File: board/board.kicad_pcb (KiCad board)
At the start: 2 copper layers, 44.3 x 82.8 mm, 20 parts, among them J1 port attiny, J10 BMS Bat +, J11 BMS Bat gnd, J12 BMS out -, J13 BMS in +5v, J14 BMS in gnd, J2 alim attiny, J24 port 3-C265421, J3 alim mp3, J4 hp mp3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

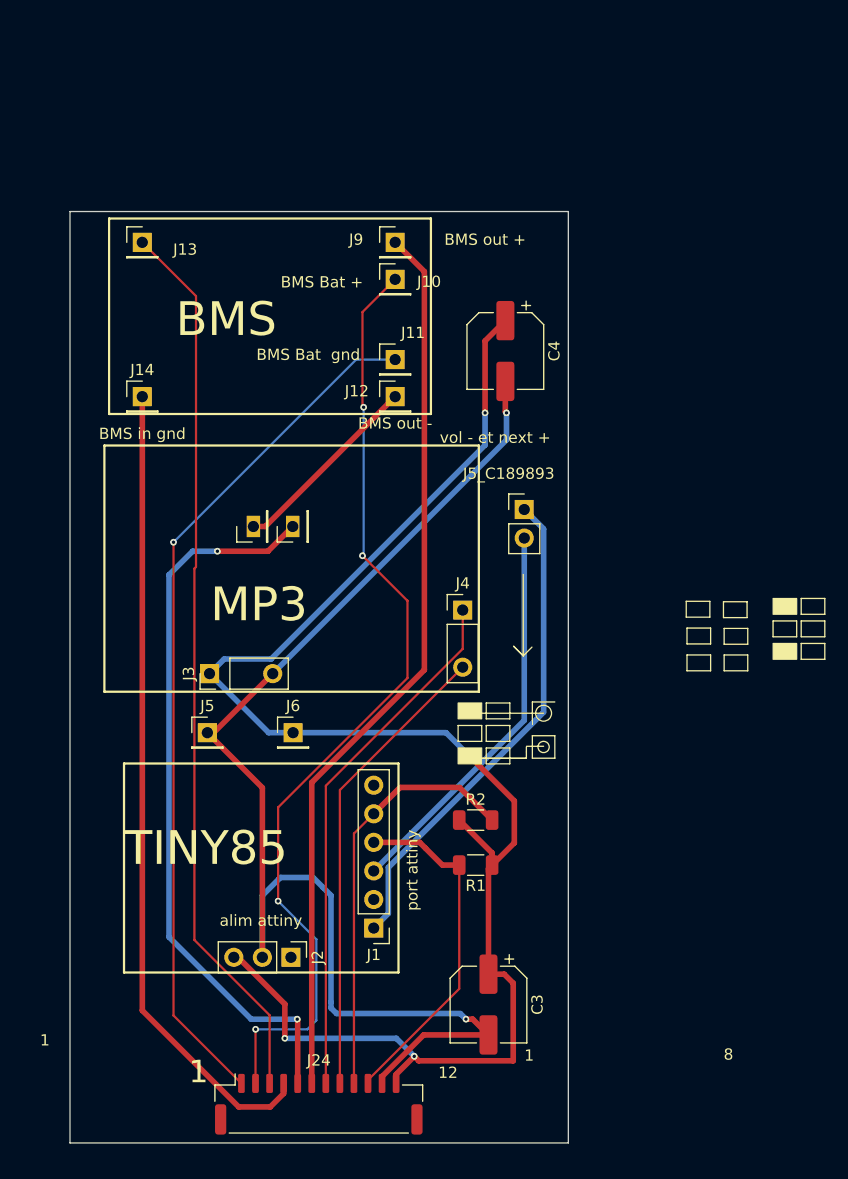
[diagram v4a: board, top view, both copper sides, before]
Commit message: mise a jour marquage pcb et ajout programation tiny dans le source
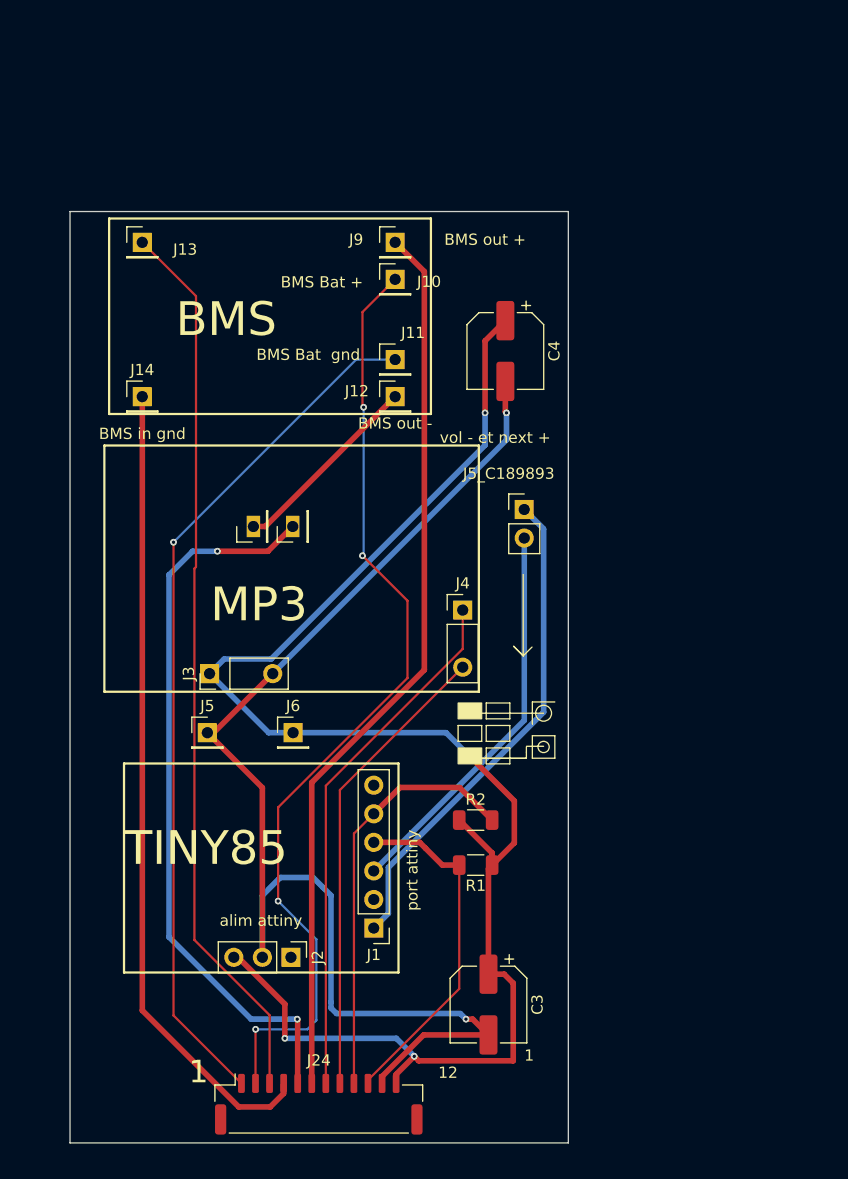
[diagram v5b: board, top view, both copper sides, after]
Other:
- board text removed: "8"
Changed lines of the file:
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@@
-		(layer "F.SilkS")
-	)
-	(gr_rect
-		(start 126.9 74.295)
-		(end 129 75.705)
-		(stroke
-			(width 0.1)
-			(type default)
-		)
-		(fill no)
 		(layer "F.SilkS")
 	)
@@
 		(layer "F.SilkS")
 	)
-	(gr_rect
-		(start 126.9 72.295)
-		(end 129 73.705)
-		(stroke
-			(width 0.1)
-			(type default)
-		)
-		(fill no)
-		(layer "F.SilkS")
-	)
-	(gr_rect
-		(start 116.75 74.93)
-		(end 118.85 76.34)
-		(stroke
-			(width 0.1)
-			(type default)
-		)
-		(fill no)
-		(layer "F.SilkS")
-	)
-	(gr_rect
-		(start 124.4 72.295)
-		(end 126.5 73.705)
-		(stroke
-			(width 0.1)
-			(type solid)
-		)
-		(fill yes)
-		(layer "F.SilkS")
-	)
 	(gr_circle
 		(center 104 82.5)
@@
 	)
 	(gr_rect
-		(start 124.4 76.295)
-		(end 126.5 77.705)
-		(stroke
-			(width 0.1)
-			(type solid)
-		)
-		(fill yes)
-		(layer "F.SilkS")
-	)
-	(gr_rect
-		(start 124.4 74.295)
-		(end 126.5 75.705)
-		(stroke
-			(width 0.1)
-			(type default)
-		)
-		(fill no)
-		(layer "F.SilkS")
-	)
-	(gr_rect
 		(start 98.9 83.59)
 		(end 101 85)
@@
 		(layer "F.SilkS")
 	)
-	(gr_rect
-		(start 120.05 77.32)
-		(end 122.15 78.73)
-		(stroke
-			(width 0.1)
-			(type default)
-		)
-		(fill no)
-		(layer "F.SilkS")
-	)
-	(gr_rect
-		(start 126.9 76.295)
-		(end 129 77.705)
-		(stroke
-			(width 0.1)
-			(type default)
-		)
-		(fill no)
-		(layer "F.SilkS")
-	)
 	(gr_line
 		(start 105 81.5)
@@
 		(layer "F.SilkS")
 	)
-	(gr_rect
-		(start 116.68 72.55)
-		(end 118.78 73.96)
-		(stroke
-			(width 0.1)
-			(type default)
-		)
-		(fill no)
-		(layer "F.SilkS")
-	)
-	(gr_rect
-		(start 116.75 77.32)
-		(end 118.85 78.73)
-		(stroke
-			(width 0.1)
-			(type default)
-		)
-		(fill no)
-		(layer "F.SilkS")
-	)
 	(gr_line
 		(start 102.47 85.95)
@@
 	)
 	(gr_rect
-		(start 119.99 72.59)
-		(end 122.09 74)
-		(stroke
-			(width 0.1)
-			(type default)
-		)
-		(fill no)
-		(layer "F.SilkS")
-	)
-	(gr_rect
 		(start 65.375 38.52)
 		(end 93.985 55.9)
@@
 		(layer "F.SilkS")
 	)
-	(gr_rect
-		(start 120.05 74.96)
-		(end 122.15 76.37)
-		(stroke
-			(width 0.1)
-			(type default)
-		)
-		(fill no)
-		(layer "F.SilkS")
-	)
 	(gr_line
 		(start 102.19 70.15)
@@
 		(layer "Edge.Cuts")
 	)
-	(gr_text "1"
-		(at 59.23 112.16 0)
-		(layer "F.SilkS")
-		(effects
-			(font
-				(size 1 1)
-				(thickness 0.1)
-			)
-			(justify left bottom)
-		)
-	)
 	(gr_text "MP3"
 		(at 74.38 74.6 0)
@@
 				(thickness 0.1)
 			)
-			(justify left bottom)
-		)
-	)
-	(gr_text "8"
-		(at 120 113.42 0)
-		(layer "F.SilkS")
-		(effects
-			(font
-				(size 1 1)
-				(thickness 0.1)
-			)

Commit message: ajout connecteur programmation tiny85
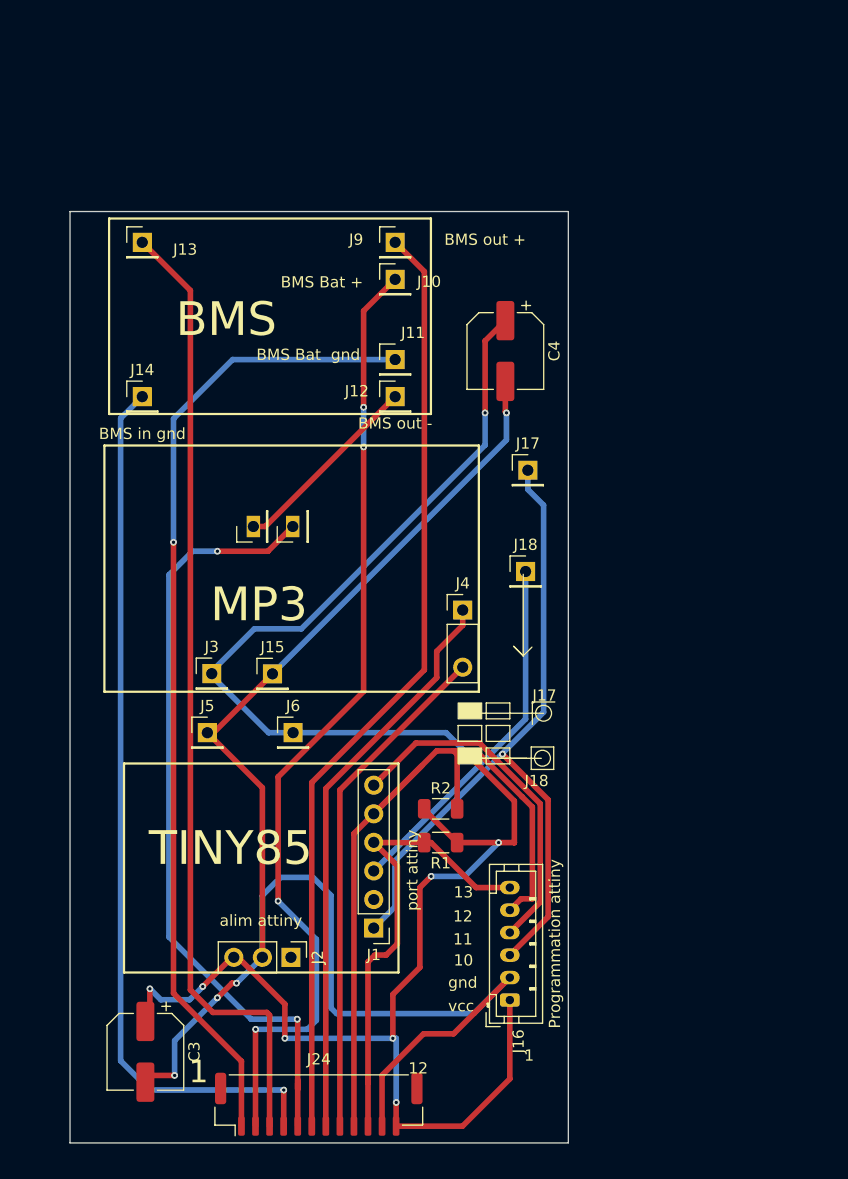
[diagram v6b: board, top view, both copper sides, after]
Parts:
- removed J5_C189893: vol - et next +, Connector_PinHeader_2.54mm:PinHeader_1x02_P2.54mm_Vertical
- added J15: alim mp3 -, Connector_PinHeader_2.54mm:PinHeader_1x01_P2.54mm_Vertical, F.Cu at (79.9, 79.0)
- added J16: Programmation attiny, Connector_JST:JST_PH_B6B-PH-K_1x06_P2.00mm_Vertical, F.Cu at (101.0, 108.0)
- added J17: next, Connector_PinHeader_2.54mm:PinHeader_1x01_P2.54mm_Vertical, F.Cu at (102.6, 60.9)
- added J18: vol -, Connector_PinHeader_2.54mm:PinHeader_1x01_P2.54mm_Vertical, F.Cu at (102.4, 69.9)
- J24: footprint Connector_JST:JST_GH_SM12B-GHS-TB_1x12-1MP_P1.25mm_Horizontal -> Connector_JST:JST_GH_BM12B-GHS-TBT_1x12-1MP_P1.25mm_Vertical
- J3: value alim mp3 -> alim mp3 +; footprint Library:PinHeader_1x03_P2.54mm_Vertical-mp3 -> Connector_PinHeader_2.54mm:PinHeader_1x01_P2.54mm_Vertical
- moved C3 30.8 mm to (68.6, 112.6)
- moved R1 3.70 mm to (94.8, 94.0)
- moved R2 3.27 mm to (94.9, 91.0)
- moved J3 0.34 mm to (74.5, 79.0), turned to 0 degrees
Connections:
- J1 pad 6: unconnected-(J1-Pin_6-Pad6) -> Net-(J1-Pin_6)
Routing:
- net Net-(J1-Pin_6): track 0.00 -> 31.2 mm
- net Net-(J1-Pin_5): track 38.1 -> 68.8 mm
- net VCC: track 141.0 -> 170.9 mm, vias 4 -> 9
- net GND: track 114.7 -> 141.8 mm, vias 2 -> 4
- net Net-(J1-Pin_1): track 44.2 -> 68.5 mm, vias 0 -> 1
- net Net-(J1-Pin_4): track 31.2 -> 42.3 mm
- net Net-(J11-Pin_1): track 77.2 -> 87.4 mm
- net Net-(J10-Pin_1): track 85.5 -> 94.4 mm
- net Net-(J14-Pin_1): track 72.8 -> 79.3 mm, vias 0 -> 1
- net Net-(J13-Pin_1): track 79.6 -> 86.1 mm
- net Net-(J24-Pin_6): track 80.7 -> 84.5 mm
- net Net-(J24-Pin_8): track 41.5 -> 45.3 mm
- net Net-(J24-Pin_7): track 47.1 -> 50.9 mm
- net Net-(J24-Pin_5): track 66.5 -> 70.3 mm
- net Net-(J1-Pin_3): track 35.1 -> 32.2 mm
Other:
- board text added: "10"
- board text added: "11"
- board text added: "13"
- board text added: "J17"
- board text added: "J18"
- board text added: "gnd"
- board text added: "vcc"
